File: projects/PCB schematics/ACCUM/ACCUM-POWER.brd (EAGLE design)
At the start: 71.1 x 46.7 mm, 8 parts, among them J1 2P(90DEG)_1-770966-0, J2 2P(90DEG)_1-770966-0, J3 2P(90DEG)_1-770966-0

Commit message: ACCUM - Rev A.
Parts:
- renumbered C11 to C3, C14 to C1, C15 to C2
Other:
- board text added: "+"
- board text added: "1. HV- 2. +15V-NONISO 3. HV+"
- board text added: "Accumulator Indicator Light Rev A: April 11th, 2019"
- board text added: "Connections:"
- board text added: "Iowa Formula"
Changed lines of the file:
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@@
 <hole x="66.04" y="41.91" drill="3"/>
 <hole x="5.08" y="41.91" drill="3"/>
+<text x="52.3494" y="21.7932" size="1.778" layer="25">+</text>
+<text x="40.6908" y="21.9964" size="1.778" layer="25">+</text>
+<text x="23.8506" y="19.2024" size="1.778" layer="25">+</text>
+<text x="2.9464" y="18.8468" size="1.016" layer="25" font="vector">Accumulator Indicator Light
+Rev A: April 11th, 2019</text>
+<wire x1="2.8194" y1="35.687" x2="2.8194" y2="25.019" width="0.1524" layer="25"/>
+<wire x1="2.8194" y1="25.019" x2="13.1318" y2="25.019" width="0.1524" layer="25"/>
+<wire x1="13.1318" y1="25.019" x2="13.1318" y2="35.687" width="0.1524" layer="25"/>
+<wire x1="13.1318" y1="35.687" x2="2.8194" y2="35.687" width="0.1524" layer="25"/>
+<wire x1="6.7818" y1="34.671" x2="3.8862" y2="25.6794" width="0.1524" layer="25"/>
+<wire x1="3.8862" y1="25.6794" x2="5.1308" y2="25.6794" width="0.1524" layer="25"/>
+<wire x1="5.1308" y1="25.6794" x2="8.0772" y2="34.671" width="0.1524" layer="25"/>
+<wire x1="8.0772" y1="34.671" x2="6.7818" y2="34.671" width="0.1524" layer="25"/>
+<wire x1="8.636" y1="34.544" x2="5.9944" y2="25.654" width="0.1524" layer="25"/>
+<wire x1="5.9944" y1="25.654" x2="7.3914" y2="25.654" width="0.1524" layer="25"/>
+<wire x1="7.3914" y1="25.654" x2="8.7376" y2="29.7688" width="0.1524" layer="25"/>
+<wire x1="8.7376" y1="29.7688" x2="10.7188" y2="29.7688" width="0.1524" layer="25"/>
+<wire x1="10.7188" y1="29.7688" x2="10.9982" y2="30.7086" width="0.1524" layer="25"/>
+<wire x1="10.9982" y1="30.7086" x2="8.6614" y2="30.7086" width="0.1524" layer="25"/>
+<wire x1="8.6614" y1="30.7086" x2="9.5758" y2="33.5534" width="0.1524" layer="25"/>
+<wire x1="9.5758" y1="33.5534" x2="11.938" y2="33.5534" width="0.1524" layer="25"/>
+<wire x1="11.938" y1="33.5534" x2="12.192" y2="34.544" width="0.1524" layer="25"/>
+<wire x1="12.192" y1="34.544" x2="8.636" y2="34.544" width="0.1524" layer="25"/>
+<text x="56.261" y="29.2608" size="1.016" layer="25" font="vector">1. HV-
+2. +15V-NONISO
+3. HV+</text>
+<text x="56.515" y="34.2646" size="1.4224" layer="25" font="vector">Connections:</text>
+<wire x1="56.388" y1="33.7566" x2="67.6402" y2="33.7566" width="0.1524" layer="25"/>
+<text x="2.8956" y="22.8092" size="1.4224" layer="25" font="vector">Iowa Formula</text>
 </plain>
 <attributes>
@@
 <attribute name="SPICEPREFIX" value="L" x="63.5" y="18.669" size="1.778" layer="27" rot="R180" display="off"/>
 </element>
-<element name="C11" library="EEU-FS1H221L" package="CAPPRD350W65D800H2200" value="EEU-FS1H221L" x="25.4" y="21.59" smashed="yes">
+<element name="C3" library="EEU-FS1H221L" package="CAPPRD350W65D800H2200" value="EEU-FS1H221L" x="25.4" y="21.59" smashed="yes">
 <attribute name="DESCRIPTION" value="Aluminum Electrolytic Capacitors - Radial Leaded 50VDC 220uF 9000H 8x20mm" x="-8.89" y="2.54" size="1.778" layer="27" display="off"/>
 <attribute name="HEIGHT" value="22mm" x="-8.89" y="2.54" size="1.778" layer="27" display="off"/>
@@
 <attribute name="RS_PRICE-STOCK" value="" x="-8.89" y="2.54" size="1.778" layer="27" display="off"/>
 </element>
-<element name="C14" library="EKXF451ELL100MJ20S" package="CAPPRD500W60D1025H2150" value="EKXF451ELL100MJ20S" x="52.959" y="24.638" smashed="yes" rot="R180">
+<element name="C1" library="EKXF451ELL100MJ20S" package="CAPPRD500W60D1025H2150" value="EKXF451ELL100MJ20S" x="52.959" y="24.638" smashed="yes" rot="R180">
 <attribute name="DESCRIPTION" value="Aluminum Electrolytic Capacitors - Radial Leaded 10uF 20% 450V Long Life" x="80.899" y="76.708" size="1.778" layer="27" rot="R180" display="off"/>
 <attribute name="HEIGHT" value="21.5mm" x="80.899" y="76.708" size="1.778" layer="27" rot="R180" display="off"/>
@@
 <attribute name="RS_PRICE-STOCK" value="" x="80.899" y="76.708" size="1.778" layer="27" rot="R180" display="off"/>
 </element>
-<element name="C15" library="EKXF451ELL100MJ20S" package="CAPPRD500W60D1025H2150" value="EKXF451ELL100MJ20S" x="41.275" y="24.638" smashed="yes" rot="R180">
+<element name="C2" library="EKXF451ELL100MJ20S" package="CAPPRD500W60D1025H2150" value="EKXF451ELL100MJ20S" x="41.275" y="24.638" smashed="yes" rot="R180">
 <attribute name="DESCRIPTION" value="Aluminum Electrolytic Capacitors - Radial Leaded 10uF 20% 450V Long Life" x="66.675" y="74.168" size="1.778" layer="27" rot="R180" display="off"/>
 <attribute name="HEIGHT" value="21.5mm" x="66.675" y="74.168" size="1.778" layer="27" rot="R180" display="off"/>
@@
 <signal name="HV-">
 <contactref element="PS1" pad="4"/>
-<contactref element="C11" pad="2"/>
-<contactref element="C15" pad="2"/>
+<contactref element="C3" pad="2"/>
+<contactref element="C2" pad="2"/>
 <contactref element="J2" pad="1"/>
 <contactref element="J2" pad="2"/>
@@
 <signal name="HV+">
 <contactref element="PS1" pad="1"/>
-<contactref element="C14" pad="1"/>
+<contactref element="C1" pad="1"/>
 <contactref element="J1" pad="1"/>
 <contactref element="J1" pad="2"/>
@@
 <signal name="+15V-NONISO">
 <contactref element="PS1" pad="10"/>
-<contactref element="C11" pad="1"/>
+<contactref element="C3" pad="1"/>
 <contactref element="J3" pad="1"/>
 <contactref element="J3" pad="2"/>
@@
 </signal>
 <signal name="N$3">
-<contactref element="C14" pad="2"/>
-<contactref element="C15" pad="1"/>
+<contactref element="C1" pad="2"/>
+<contactref element="C2" pad="1"/>
 <wire x1="41.275" y1="24.638" x2="47.959" y2="24.638" width="0.8128" layer="1"/>
 </signal>
@@
 </drawing>
 <compatibility>
+<note version="6.3" minversion="6.2.2" severity="warning">
+Since Version 6.2.2 text objects can contain more than one line,
+which will not be processed correctly with this version.
+</note>
 <note version="8.2" severity="warning">
 Since Version 8.2, EAGLE supports online libraries. The ids

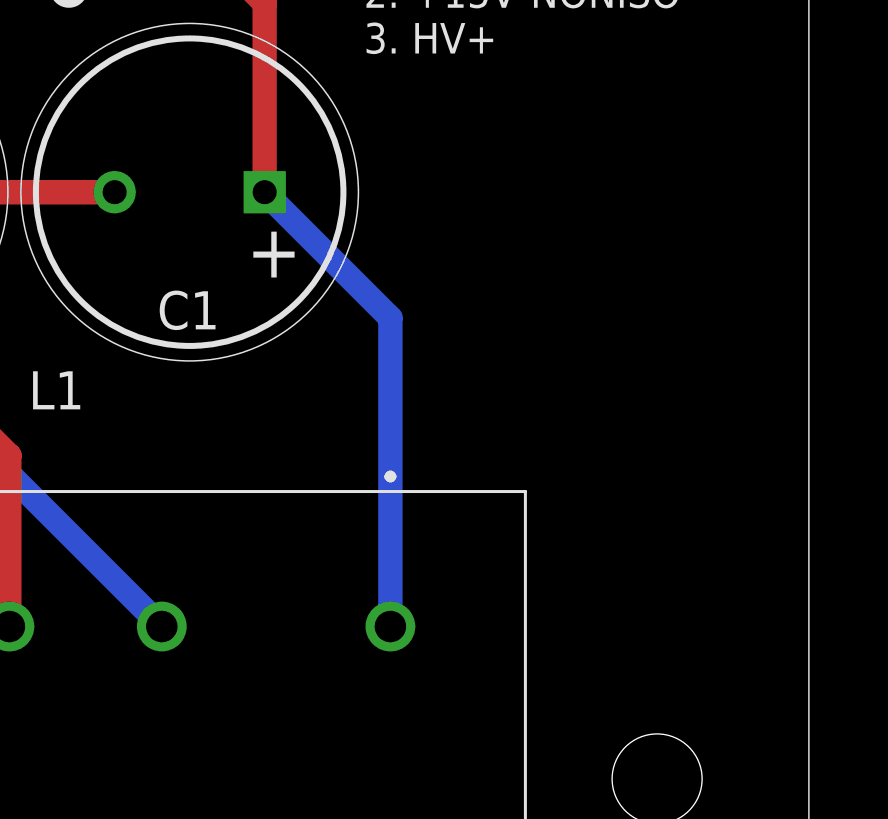
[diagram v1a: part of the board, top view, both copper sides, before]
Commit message: TSAL - Added in fuses.
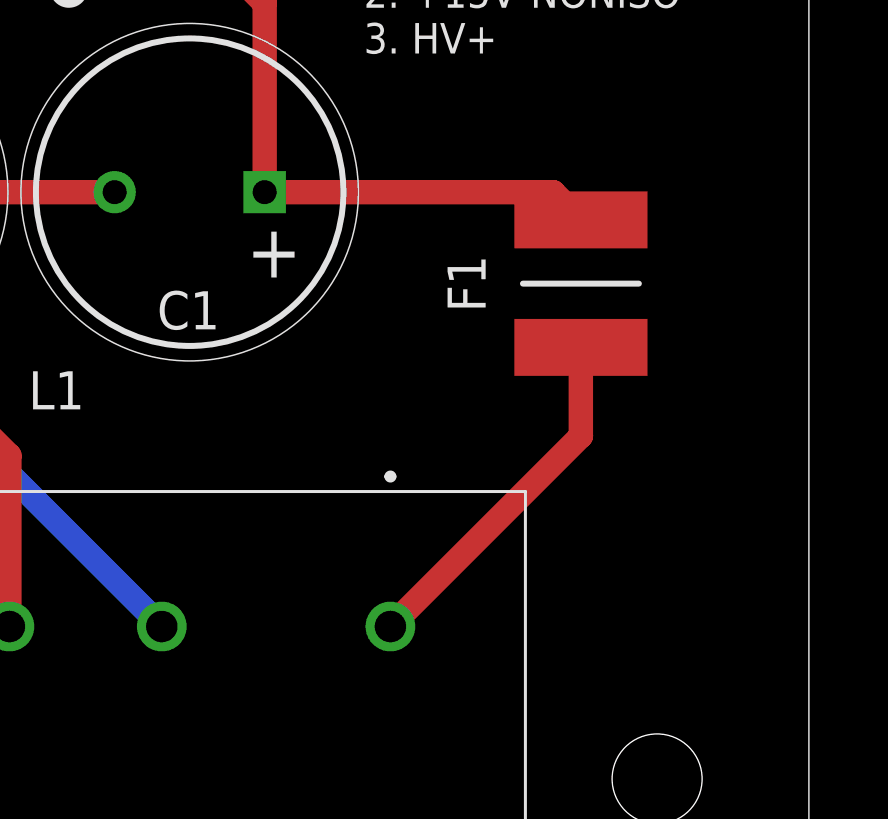
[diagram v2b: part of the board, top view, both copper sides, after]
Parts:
- added F1: 2016L030DR, SamacSys_Parts:FUSC5141X125N
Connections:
- new net N$4: F1.2, PS1.1
- net HV+: now also F1.1; no longer PS1.1
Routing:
- net N$4: track 0.00 -> 11.9 mm
- net HV+: track 30.0 -> 24.7 mm
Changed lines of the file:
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@@
 <?xml version="1.0" encoding="utf-8"?>
 <!DOCTYPE eagle SYSTEM "eagle.dtd">
-<eagle version="9.3.2">
+<eagle version="9.4.0">
 <drawing>
 <settings>
@@
 <attribute name="VENDOR" value="TE Connectivity" x="23.876" y="49.784" size="1.778" layer="27" display="off"/>
 </element>
+<element name="F1" library="SamacSys_Parts" package="FUSC5141X125N" value="2016L030DR" x="63.5" y="21.59" smashed="yes" rot="R270">
+<attribute name="DESCRIPTION" value="Littelfuse 0.3A Surface Mount Resettable Fuse, 60 V dc" x="63.5" y="21.59" size="1.778" layer="27" rot="R270" display="off"/>
+<attribute name="HEIGHT" value="1.25mm" x="63.5" y="21.59" size="1.778" layer="27" rot="R270" display="off"/>
+<attribute name="MANUFACTURER_NAME" value="LITTELFUSE" x="63.5" y="21.59" size="1.778" layer="27" rot="R270" display="off"/>
+<attribute name="MANUFACTURER_PART_NUMBER" value="2016L030DR" x="63.5" y="21.59" size="1.778" layer="27" rot="R270" display="off"/>
+<attribute name="MOUSER_PART_NUMBER" value="576-2016L030DR" x="63.5" y="21.59" size="1.778" layer="27" rot="R270" display="off"/>
+<attribute name="MOUSER_PRICE-STOCK" value="https://www.mouser.com/Search/Refine.aspx?Keyword=576-2016L030DR" x="63.5" y="21.59" size="1.778" layer="27" rot="R270" display="off"/>
+<attribute name="NAME" x="59.69" y="21.59" size="1.27" layer="25" rot="R270" align="center"/>
+<attribute name="VALUE" x="67.31" y="20.32" size="1.27" layer="27" rot="R270" align="center"/>
+</element>
 </elements>
 <signals>
@@
 </signal>
 <signal name="HV+">
-<contactref element="PS1" pad="1"/>
 <contactref element="C1" pad="1"/>
 <contactref element="J1" pad="1"/>
 <contactref element="J1" pad="2"/>
-<wire x1="52.959" y1="24.638" x2="57.15" y2="20.447" width="0.8128" layer="16"/>
-<wire x1="57.15" y1="20.447" x2="57.15" y2="10.16" width="0.8128" layer="16"/>
 <wire x1="50.5714" y1="33.3248" x2="46.4312" y2="33.3248" width="1.27" layer="1"/>
 <wire x1="50.5714" y1="33.3248" x2="52.959" y2="30.9372" width="0.8128" layer="1"/>
 <wire x1="52.959" y1="30.9372" x2="52.959" y2="24.638" width="0.8128" layer="1"/>
+<contactref element="F1" pad="1"/>
+<wire x1="52.959" y1="24.638" x2="62.577" y2="24.638" width="0.8128" layer="1"/>
+<wire x1="62.577" y1="24.638" x2="63.5" y2="23.715" width="0.8128" layer="1"/>
 </signal>
 <signal name="N$1">
@@
 <wire x1="41.275" y1="24.638" x2="47.959" y2="24.638" width="0.8128" layer="1"/>
 </signal>
+<signal name="N$4">
+<contactref element="F1" pad="2"/>
+<contactref element="PS1" pad="1"/>
+<wire x1="63.5" y1="19.465" x2="63.5" y2="16.51" width="0.8128" layer="1"/>
+<wire x1="63.5" y1="16.51" x2="57.15" y2="10.16" width="0.8128" layer="1"/>
+</signal>
 </signals>

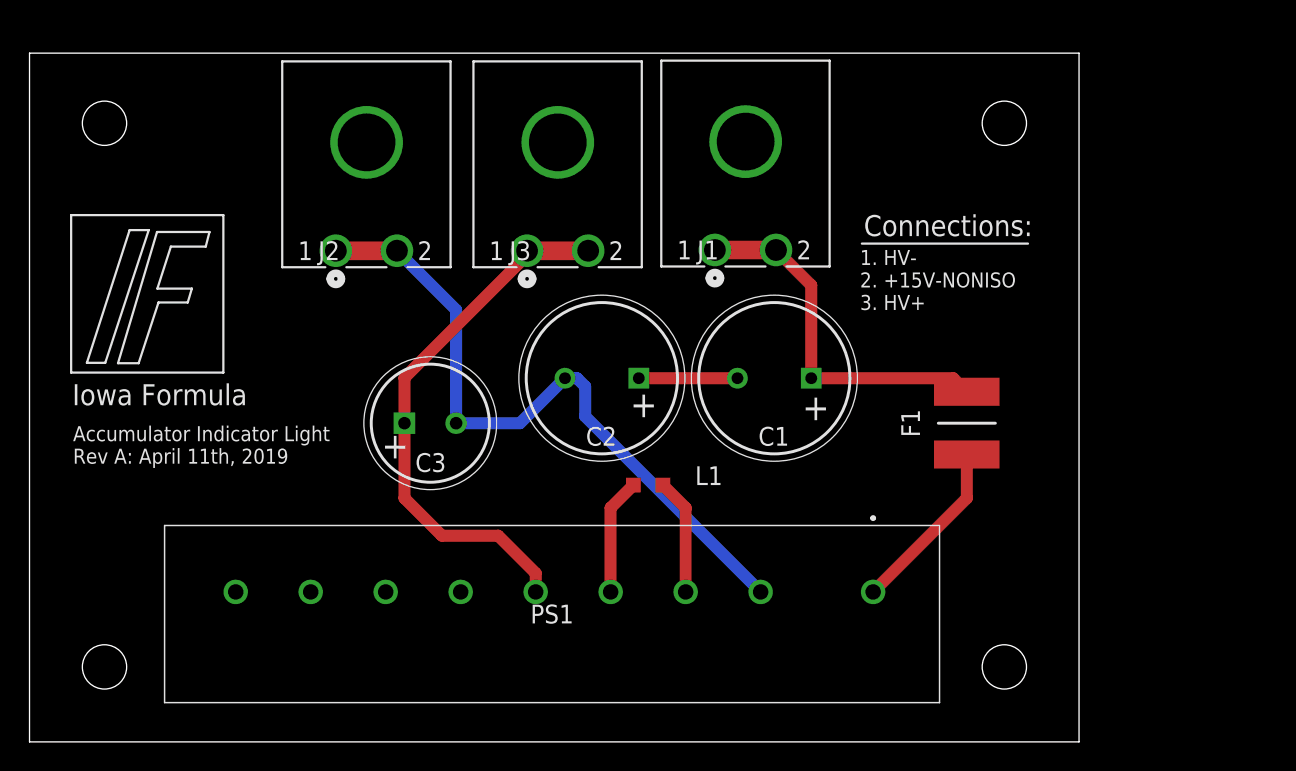
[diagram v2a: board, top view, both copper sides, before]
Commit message: TSAL - Added in fuses.
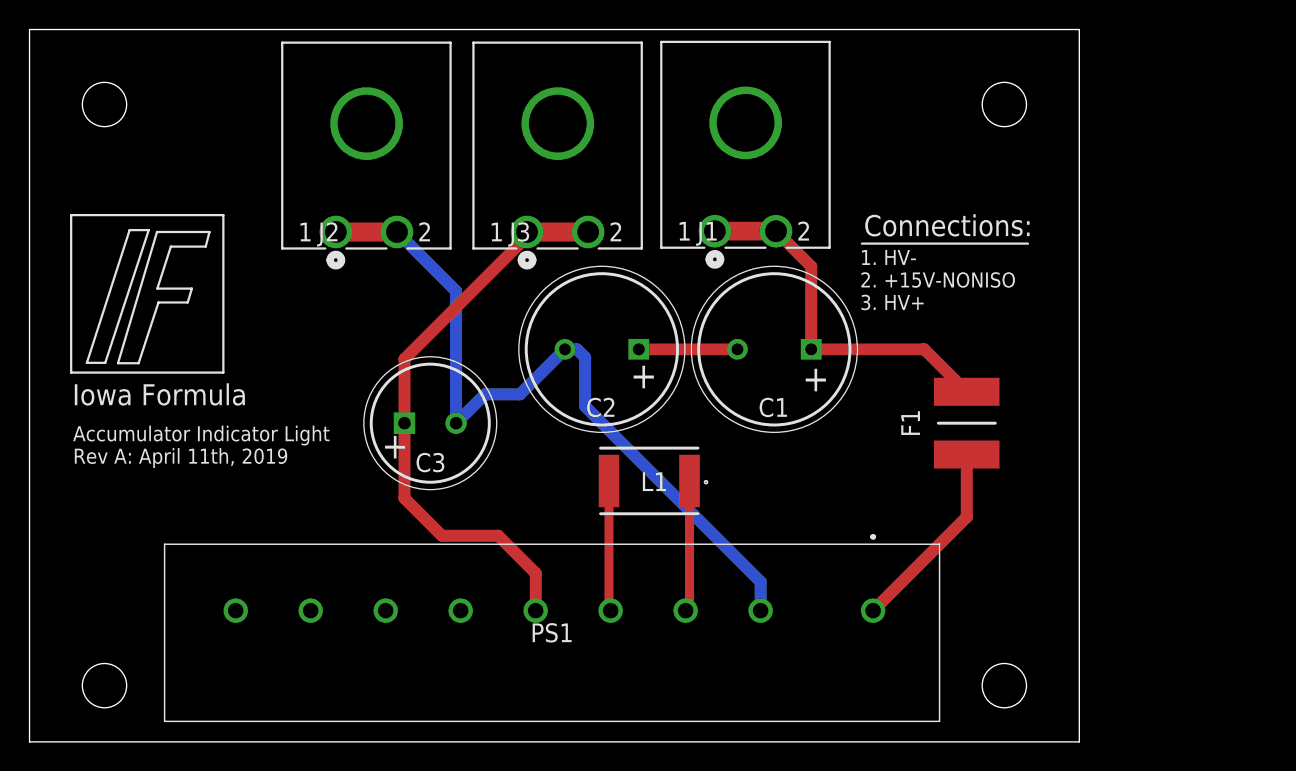
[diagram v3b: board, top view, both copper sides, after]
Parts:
- L1: value 1mH -> SDE6603-102M; device rcl:L2012C -> SDE6603-102M:SDE6603
- moved C1 1.96 mm to (53.0, 26.6)
- moved C2 1.96 mm to (41.3, 26.6)
- moved PS1 1.27 mm to (57.1, 8.89)
- moved J1 1.27 mm to (50.6, 34.6)
- moved J2 1.27 mm to (24.9, 34.5)
- moved J3 1.27 mm to (37.8, 34.5)
- moved L1 0.29 mm to (42.0, 17.7)
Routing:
- net HV-: track 46.6 -> 51.9 mm
- net +15V-NONISO: track 36.6 -> 39.1 mm
- net N$4: track 11.9 -> 13.2 mm
- net N$2: track 7.88 -> 8.90 mm
- net N$1: track 7.88 -> 8.84 mm
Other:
- board size 71.1 x 46.7 mm -> 71.1 x 48.3 mm

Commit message: ACCUM - Added IMD fuses.
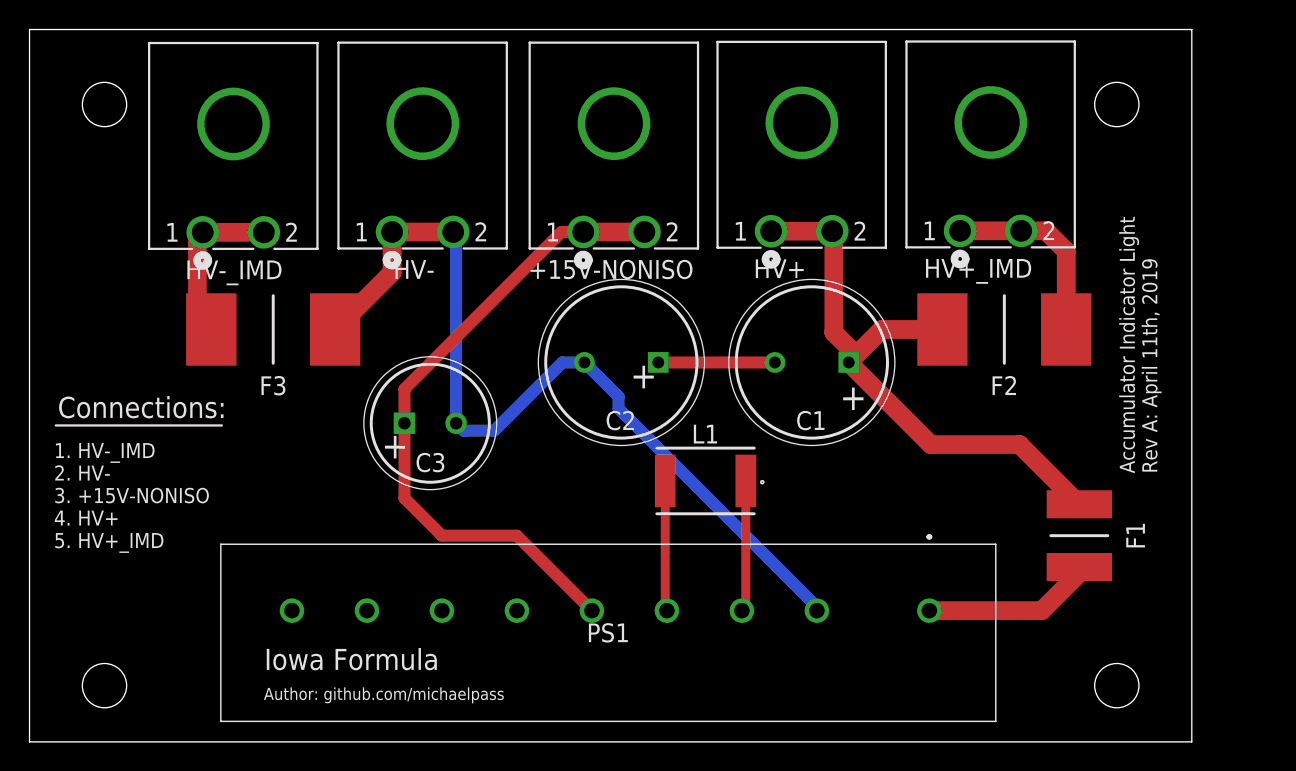
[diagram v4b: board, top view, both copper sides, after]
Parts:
- removed J1, J2, J3: 2P(90DEG)_1-770966-0, con-MATE-N-LOK:CON2_1X2_P163_RAMNL
- added +15V-NONISO, HV+, HV+_IMD, HV-, HV-_IMD: 2P(90DEG)_1-770966-0, con-MATE-N-LOK:CON2_1X2_P163_RAMNL
- added F2, F3: 0885001.DR, 0885001.DR:FUSC10948X488N
- moved F1 10.8 mm to (71.1, 14.0)
- moved L1 3.81 mm to (45.8, 17.7)
- moved PS1 3.81 mm to (61.0, 8.89)
- moved C1 2.69 mm to (55.5, 25.7)
- moved C2 1.59 mm to (42.6, 25.7)
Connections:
- new net HV+_IMD: F2.2, HV+_IMD.1, HV+_IMD.2
- new net HV-_IMD: F3.2, HV-_IMD.1, HV-_IMD.2
- net +15V-NONISO: now also +15V-NONISO.1, +15V-NONISO.2; no longer J3.1, J3.2
- net HV+: now also F2.1, HV+.1, HV+.2; no longer J1.1, J1.2
- net HV-: now also F3.1, HV-.1, HV-.2; no longer J2.1, J2.2
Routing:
- net HV+: track 24.9 -> 40.4 mm
- net HV+_IMD: track 0.00 -> 13.1 mm
- net HV-_IMD: track 0.00 -> 11.3 mm
- net HV-: track 51.9 -> 59.5 mm
- net +15V-NONISO: track 39.1 -> 43.9 mm
- net N$4: track 13.2 -> 11.6 mm
- net N$3: track 6.68 -> 7.90 mm
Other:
- board size 71.1 x 48.3 mm -> 78.7 x 48.3 mm
- board text added: "1. HV-_IMD 2. HV- 3. +15V-NONISO 4. HV+ 5. HV+_IMD"
- board text added: "Author: github.com/michaelpass"
- board text removed: "1. HV- 2. +15V-NONISO 3. HV+"

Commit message: PROJ - Final pre-purchase revisions (4 boards still in progress.)
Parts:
- moved C2 2.54 mm to (45.1, 25.7)
- moved C3 2.54 mm to (27.9, 21.6)
- moved +15V-NONISO 2.54 mm to (44.2, 34.5)
- moved C1 2.54 mm to (58.0, 25.7)
- moved F3 2.54 mm to (19.1, 27.9)
- moved HV+ 2.54 mm to (56.9, 34.6)
- moved HV- 2.54 mm to (31.2, 34.5)
- moved HV-_IMD 2.54 mm to (18.4, 34.5)
- moved L1 2.54 mm to (48.3, 17.7)
- moved PS1 2.54 mm to (63.5, 8.89)
- moved F1 2.54 mm to (73.7, 14.0)
- moved F2 2.54 mm to (68.6, 27.9)
- moved HV+_IMD 2.54 mm to (69.7, 34.6)
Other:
- board size 78.7 x 48.3 mm -> 83.8 x 48.3 mm

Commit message: PROJ - Gerber files major milestone - 05/05/19.
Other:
- board text added: "Accumulator Indicator Light Rev A: May 5th, 2019"
- board text removed: "Accumulator Indicator Light Rev A: April 11th, 2019"
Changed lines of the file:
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@@
 <wire x1="83.82" y1="48.26" x2="0" y2="48.26" width="0" layer="20"/>
 <wire x1="0" y1="48.26" x2="0" y2="0" width="0" layer="20"/>
-<hole x="5.08" y="3.81" drill="3"/>
-<hole x="78.74" y="3.81" drill="3"/>
+<hole x="5.08" y="5.08" drill="3"/>
+<hole x="78.74" y="5.08" drill="3"/>
 <hole x="78.74" y="43.18" drill="3"/>
 <hole x="5.08" y="43.18" drill="3"/>
@@
 <text x="26.3906" y="19.2024" size="1.778" layer="25">+</text>
 <text x="81.4832" y="18.1864" size="1.016" layer="25" font="vector" rot="R90">Accumulator Indicator Light
-Rev A: April 11th, 2019</text>
+Rev A: May 5th, 2019</text>
 <text x="1.651" y="13.1318" size="1.016" layer="25" font="vector">1. HV-_IMD
 2. HV-
